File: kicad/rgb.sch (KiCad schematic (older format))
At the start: 3 parts, among them Q1 PMV15ENEA, Q2 PMV15ENEA, U1 ATTINY404-SSNR

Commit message: Starting schematics
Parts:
- removed Q1, Q2: PMV15ENEA, Package_TO_SOT_SMD:SOT-23_Handsoldering, symbol Device:Q_NMOS_GSD
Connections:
- net labels removed: DRAIN_1, DRAIN_2, GND, PWM_1, PWM_2
- wire segments 8 -> 0
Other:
- moved on the sheet: U1
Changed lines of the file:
@@
 Comment4 ""
 $EndDescr
-Wire Wire Line
-	5500 1350 5500 1400
-$Comp
-L power:GND #PWR0101
-U 1 1 5FE3CA70
-P 5500 1400
-F 0 "#PWR0101" H 5500 1150 50  0001 C CNN
-F 1 "GND" H 5505 1227 50  0000 C CNN
-F 2 "" H 5500 1400 50  0001 C CNN
-F 3 "" H 5500 1400 50  0001 C CNN
-	1    5500 1400
-	1    0    0    -1
-$EndComp
-Wire Wire Line
-	5500 950  5500 900
-Wire Wire Line
-	5500 900  6000 900
-Text Label 6000 900  2    50   ~ 0
-DRAIN_1
-Wire Wire Line
-	5500 2350 5500 2400
-$Comp
-L power:GND #PWR0102
-U 1 1 5FE3FFDC
-P 5500 2400
-F 0 "#PWR0102" H 5500 2150 50  0001 C CNN
-F 1 "GND" H 5505 2227 50  0000 C CNN
-F 2 "" H 5500 2400 50  0001 C CNN
-F 3 "" H 5500 2400 50  0001 C CNN
-	1    5500 2400
-	1    0    0    -1
-$EndComp
-Wire Wire Line
-	5500 1950 5500 1900
-Wire Wire Line
-	5500 1900 6000 1900
-Text Label 6000 1900 2    50   ~ 0
-DRAIN_2
-Wire Wire Line
-	4900 2150 5200 2150
-Text Label 4900 2150 0    50   ~ 0
-PWM_2
-$Comp
-L Device:Q_NMOS_GSD Q2
-U 1 1 5FE3FFD3
-P 5400 2150
-F 0 "Q2" H 5605 2196 50  0000 L CNN
-F 1 "PMV15ENEA" H 5605 2105 50  0000 L CNN
-F 2 "Package_TO_SOT_SMD:SOT-23_Handsoldering" H 5600 2250 50  0001 C CNN
-F 3 "https://assets.nexperia.com/documents/data-sheet/PMV15ENEA.pdf" H 5400 2150 50  0001 C CNN
-	1    5400 2150
-	1    0    0    -1
-$EndComp
-Wire Wire Line
-	4900 1150 5200 1150
-Text Label 4900 1150 0    50   ~ 0
-PWM_1
-$Comp
-L Device:Q_NMOS_GSD Q1
-U 1 1 5FE256DE
-P 5400 1150
-F 0 "Q1" H 5605 1196 50  0000 L CNN
-F 1 "PMV15ENEA" H 5605 1105 50  0000 L CNN
-F 2 "Package_TO_SOT_SMD:SOT-23_Handsoldering" H 5600 1250 50  0001 C CNN
-F 3 "https://assets.nexperia.com/documents/data-sheet/PMV15ENEA.pdf" H 5400 1150 50  0001 C CNN
-	1    5400 1150
-	1    0    0    -1
-$EndComp
 $Comp
 L ATTINY404-SSNR:ATTINY404-SSNR U1
 U 1 1 5FE13C65
-P 1490 1450
-F 0 "U1" H 2690 1937 60  0000 C CNN
-F 1 "ATTINY404-SSNR" H 2690 1831 60  0000 C CNN
-F 2 "rgb_footprints:ATTINY404-SSNR" H 2690 1790 60  0001 C CNN
-F 3 "https://ww1.microchip.com/downloads/en/DeviceDoc/ATtiny204-404-DataSheet-DS50002687B.pdf" H 2690 1831 60  0001 C CNN
-	1    1490 1450
+P 840 1600
+F 0 "U1" H 2040 2087 60  0000 C CNN
+F 1 "ATTINY404-SSNR" H 2040 1981 60  0000 C CNN
+F 2 "rgb_footprints:ATTINY404-SSNR" H 2040 1940 60  0001 C CNN
+F 3 "https://ww1.microchip.com/downloads/en/DeviceDoc/ATtiny204-404-DataSheet-DS50002687B.pdf" H 2040 1981 60  0001 C CNN
+	1    840  1600
 	1    0    0    -1
 $EndComp

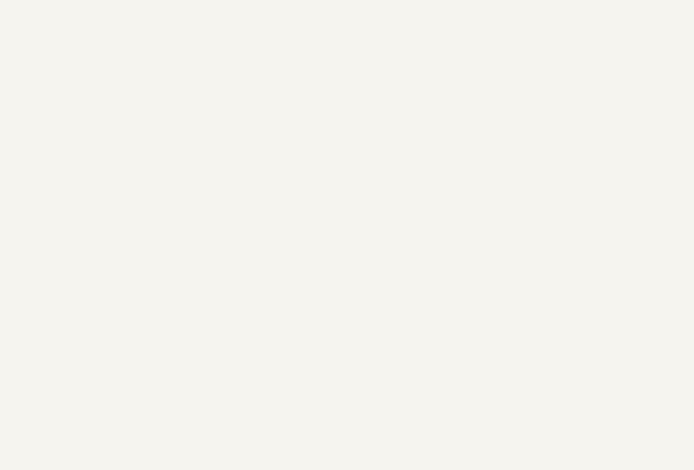
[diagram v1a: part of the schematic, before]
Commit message: changed mosfets
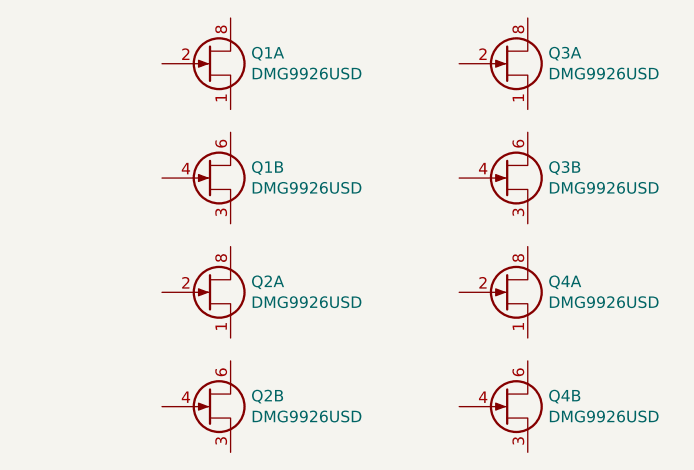
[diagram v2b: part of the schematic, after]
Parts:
- added Q1, Q2, Q3, Q4: DMG9926USD, Package_SO:SO-8_3.9x4.9mm_P1.27mm, symbol mosfet:DMG9926USD
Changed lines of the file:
@@
+	1    0    0    -1
+$EndComp
+$Comp
+L mosfet:DMG9926USD Q1
+U 1 1 5FE90B41
+P 4950 1000
+F 0 "Q1" H 5090 1046 50  0000 L CNN
+F 1 "DMG9926USD" H 5090 955 50  0000 L CNN
+F 2 "Package_SO:SO-8_3.9x4.9mm_P1.27mm" H 4850 500 50  0001 C CNN
+F 3 "https://www.diodes.com/assets/Datasheets/ds31757.pdf" H 4375 1160 50  0001 C CNN
+	1    4950 1000
+	1    0    0    -1
+$EndComp
+$Comp
+L mosfet:DMG9926USD Q1
+U 2 1 5FE91CF3
+P 4950 1500
+F 0 "Q1" H 5090 1546 50  0000 L CNN
+F 1 "DMG9926USD" H 5090 1455 50  0000 L CNN
+F 2 "Package_SO:SO-8_3.9x4.9mm_P1.27mm" H 4850 1000 50  0001 C CNN
+F 3 "https://www.diodes.com/assets/Datasheets/ds31757.pdf" H 4375 1660 50  0001 C CNN
+	2    4950 1500
+	1    0    0    -1
+$EndComp
+$Comp
+L mosfet:DMG9926USD Q2
+U 1 1 5FE99194
+P 4950 2000
+F 0 "Q2" H 5090 2046 50  0000 L CNN
+F 1 "DMG9926USD" H 5090 1955 50  0000 L CNN
+F 2 "Package_SO:SO-8_3.9x4.9mm_P1.27mm" H 4850 1500 50  0001 C CNN
+F 3 "https://www.diodes.com/assets/Datasheets/ds31757.pdf" H 4375 2160 50  0001 C CNN
+	1    4950 2000
+	1    0    0    -1
+$EndComp
+$Comp
+L mosfet:DMG9926USD Q2
+U 2 1 5FE9919A
+P 4950 2500
+F 0 "Q2" H 5090 2546 50  0000 L CNN
+F 1 "DMG9926USD" H 5090 2455 50  0000 L CNN
+F 2 "Package_SO:SO-8_3.9x4.9mm_P1.27mm" H 4850 2000 50  0001 C CNN
+F 3 "https://www.diodes.com/assets/Datasheets/ds31757.pdf" H 4375 2660 50  0001 C CNN
+	2    4950 2500
+	1    0    0    -1
+$EndComp
+$Comp
+L mosfet:DMG9926USD Q3
+U 1 1 5FE9AB06
+P 6250 1000
+F 0 "Q3" H 6390 1046 50  0000 L CNN
+F 1 "DMG9926USD" H 6390 955 50  0000 L CNN
+F 2 "Package_SO:SO-8_3.9x4.9mm_P1.27mm" H 6150 500 50  0001 C CNN
+F 3 "https://www.diodes.com/assets/Datasheets/ds31757.pdf" H 5675 1160 50  0001 C CNN
+	1    6250 1000
+	1    0    0    -1
+$EndComp
+$Comp
+L mosfet:DMG9926USD Q3
+U 2 1 5FE9AB0C
+P 6250 1500
+F 0 "Q3" H 6390 1546 50  0000 L CNN
+F 1 "DMG9926USD" H 6390 1455 50  0000 L CNN
+F 2 "Package_SO:SO-8_3.9x4.9mm_P1.27mm" H 6150 1000 50  0001 C CNN
+F 3 "https://www.diodes.com/assets/Datasheets/ds31757.pdf" H 5675 1660 50  0001 C CNN
+	2    6250 1500
+	1    0    0    -1
+$EndComp
+$Comp
+L mosfet:DMG9926USD Q4
+U 1 1 5FEA036A
+P 6250 2000
+F 0 "Q4" H 6390 2046 50  0000 L CNN
+F 1 "DMG9926USD" H 6390 1955 50  0000 L CNN
+F 2 "Package_SO:SO-8_3.9x4.9mm_P1.27mm" H 6150 1500 50  0001 C CNN
+F 3 "https://www.diodes.com/assets/Datasheets/ds31757.pdf" H 5675 2160 50  0001 C CNN
+	1    6250 2000
+	1    0    0    -1
+$EndComp
+$Comp
+L mosfet:DMG9926USD Q4
+U 2 1 5FEA0370
+P 6250 2500
+F 0 "Q4" H 6390 2546 50  0000 L CNN
+F 1 "DMG9926USD" H 6390 2455 50  0000 L CNN
+F 2 "Package_SO:SO-8_3.9x4.9mm_P1.27mm" H 6150 2000 50  0001 C CNN
+F 3 "https://www.diodes.com/assets/Datasheets/ds31757.pdf" H 5675 2660 50  0001 C CNN
+	2    6250 2500
 	1    0    0    -1
 $EndComp

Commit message: Added power supply
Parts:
- added C1: 10 uF, symbol Device:C_Small
- added C2, C5: 22 uF, symbol Device:C_Small
- added C3: 100 nF, symbol Device:C_Small
- added C4: 100 pF, symbol Device:C_Small
- added L1: 2.2 uF, symbol Device:L_Small
- added R1: 30.9 kΩ, symbol Device:R_Small_US
- added R2: 62 kΩ, symbol Device:R_Small_US
- added U2: AP63205WU-7, SOIC_05WU-7_DIO, symbol AP63205WU:AP63205WU-7
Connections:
- net labels added: GND
- wire segments 0 -> 30
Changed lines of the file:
@@
 	1    0    0    -1
 $EndComp
+$Comp
+L AP63205WU:AP63205WU-7 U2
+U 1 1 5FE8CD56
+P 1650 3450
+F 0 "U2" H 2450 3837 60  0000 C CNN
+F 1 "AP63205WU-7" H 2450 3731 60  0000 C CNN
+F 2 "SOIC_05WU-7_DIO" H 2450 3690 60  0001 C CNN
+F 3 "" H 1650 3450 60  0000 C CNN
+	1    1650 3450
+	1    0    0    -1
+$EndComp
+$Comp
+L Device:R_Small_US R1
+U 1 1 5FE9900A
+P 4600 3400
+F 0 "R1" H 4500 3400 50  0000 R CNN
+F 1 "30.9 kΩ" H 4550 3500 50  0000 R CNN
+F 2 "" H 4600 3400 50  0001 C CNN
+F 3 "~" H 4600 3400 50  0001 C CNN
+	1    4600 3400
+	-1   0    0    1
+$EndComp
+$Comp
+L Device:R_Small_US R2
+U 1 1 5FE9EA80
+P 4600 3750
+F 0 "R2" H 4700 3800 50  0000 L CNN
+F 1 "62 kΩ" H 4668 3705 50  0000 L CNN
+F 2 "" H 4600 3750 50  0001 C CNN
+F 3 "~" H 4600 3750 50  0001 C CNN
+	1    4600 3750
+	1    0    0    -1
+$EndComp
+$Comp
+L Device:C_Small C1
+U 1 1 5FEA05BD
+P 1300 3700
+F 0 "C1" H 1209 3654 50  0000 R CNN
+F 1 "10 uF" H 1209 3745 50  0000 R CNN
+F 2 "" H 1300 3700 50  0001 C CNN
+F 3 "~" H 1300 3700 50  0001 C CNN
+	1    1300 3700
+	1    0    0    1
+$EndComp
+$Comp
+L Device:C_Small C3
+U 1 1 5FEA2171
+P 3400 3500
+F 0 "C3" H 3600 3600 50  0000 L CNN
+F 1 "100 nF" H 3500 3500 50  0000 L CNN
+F 2 "" H 3400 3500 50  0001 C CNN
+F 3 "~" H 3400 3500 50  0001 C CNN
+	1    3400 3500
+	1    0    0    -1
+$EndComp
+$Comp
+L Device:C_Small C2
+U 1 1 5FEA65A3
+P 5050 3600
+F 0 "C2" H 5200 3650 50  0000 C CNN
+F 1 "22 uF" H 5142 3555 50  0000 L CNN
+F 2 "" H 5050 3600 50  0001 C CNN
+F 3 "~" H 5050 3600 50  0001 C CNN
+	1    5050 3600
+	1    0    0    -1
+$EndComp
+$Comp
+L Device:L_Small L1
+U 1 1 5FEA81A8
+P 3950 3600
+F 0 "L1" V 4150 3550 50  0000 C CNN
+F 1 "2.2 uF" V 4050 3550 50  0000 C CNN
+F 2 "" H 3950 3600 50  0001 C CNN
+F 3 "~" H 3950 3600 50  0001 C CNN
+	1    3950 3600
+	0    -1   -1   0
+$EndComp
+Wire Wire Line
+	3250 3450 3250 3400
+Wire Wire Line
+	3250 3400 3400 3400
+Wire Wire Line
+	3250 3550 3250 3600
+Wire Wire Line
+	3250 3600 3400 3600
+Wire Wire Line
+	3400 3600 3850 3600
+Connection ~ 3400 3600
+Wire Wire Line
+	4050 3600 4150 3600
+Wire Wire Line
+	4150 3200 1550 3200
+Wire Wire Line
+	1550 3200 1550 3450
+Wire Wire Line
+	1550 3450 1650 3450
+Wire Wire Line
+	4150 3300 4150 3200
+$Comp
+L Device:C_Small C4
+U 1 1 5FEA44F3
+P 4150 3400
+F 0 "C4" H 4300 3400 50  0000 L CNN
+F 1 "100 pF" H 4250 3300 50  0000 L CNN
+F 2 "" H 4150 3400 50  0001 C CNN
+F 3 "~" H 4150 3400 50  0001 C CNN
+	1    4150 3400
+	1    0    0    -1
+$EndComp
+Wire Wire Line
+	4150 3600 4150 3500
+Wire Wire Line
+	4600 3300 4600 3200
+Wire Wire Line
+	4600 3200 4150 3200
+Connection ~ 4150 3200
+Wire Wire Line
+	4600 3500 4600 3600
+Wire Wire Line
+	4600 3600 4150 3600
+Connection ~ 4150 3600
+Wire Wire Line
+	4600 3600 4600 3650
+Connection ~ 4600 3600
+Wire Wire Line
+	4600 3850 4600 3900
+Wire Wire Line
+	3250 3900 3250 3650
+Wire Wire Line
+	5050 3900 5050 3700
+Wire Wire Line
+	5050 3500 5050 3200
+Wire Wire Line
+	5050 3200 4600 3200
+Connection ~ 4600 3200
+$Comp
+L power:GND #PWR?
+U 1 1 5FEC6718
+P 4600 3900
+F 0 "#PWR?" H 4600 3650 50  0001 C CNN
+F 1 "GND" H 4605 3727 50  0000 C CNN
+F 2 "" H 4600 3900 50  0001 C CNN
+F 3 "" H 4600 3900 50  0001 C CNN
+	1    4600 3900
+	1    0    0    -1
+$EndComp
+$Comp
+L power:GND #PWR?
+U 1 1 5FEC75F4
+P 1300 3900
+F 0 "#PWR?" H 1300 3650 50  0001 C CNN
+F 1 "GND" H 1305 3727 50  0000 C CNN
+F 2 "" H 1300 3900 50  0001 C CNN
+F 3 "" H 1300 3900 50  0001 C CNN
+	1    1300 3900
+	1    0    0    -1
+$EndComp
+Wire Wire Line
+	1300 3600 1300 3550
+Wire Wire Line
+	1300 3550 1600 3550
+Wire Wire Line
+	1600 3550 1600 3650
+Wire Wire Line
+	1600 3650 1650 3650
+Connection ~ 1600 3550
+Wire Wire Line
+	1600 3550 1650 3550
+$Comp
+L power:GND #PWR?
+U 1 1 5FEC9F13
+P 3250 3900
+F 0 "#PWR?" H 3250 3650 50  0001 C CNN
+F 1 "GND" H 3255 3727 50  0000 C CNN
+F 2 "" H 3250 3900 50  0001 C CNN
+F 3 "" H 3250 3900 50  0001 C CNN
+	1    3250 3900
+	1    0    0    -1
+$EndComp
+Wire Wire Line
+	1300 3800 1300 3900
+$Comp
+L power:GND #PWR?
+U 1 1 5FECCA07
+P 5050 3900
+F 0 "#PWR?" H 5050 3650 50  0001 C CNN
+F 1 "GND" H 5055 3727 50  0000 C CNN
+F 2 "" H 5050 3900 50  0001 C CNN
+F 3 "" H 5050 3900 50  0001 C CNN
+	1    5050 3900
+	1    0    0    -1
+$EndComp
+$Comp
+L Device:C_Small C5
+U 1 1 5FEDA42E
+P 5450 3600
+F 0 "C5" H 5550 3650 50  0000 L CNN
+F 1 "22 uF" H 5542 3555 50  0000 L CNN
+F 2 "" H 5450 3600 50  0001 C CNN
+F 3 "~" H 5450 3600 50  0001 C CNN
+	1    5450 3600
+	1    0    0    -1
+$EndComp
+Wire Wire Line
+	5450 3900 5450 3700
+Wire Wire Line
+	5450 3500 5450 3200
+Wire Wire Line
+	5450 3200 5050 3200
+$Comp
+L power:GND #PWR?
+U 1 1 5FEDA437
+P 5450 3900
+F 0 "#PWR?" H 5450 3650 50  0001 C CNN
+F 1 "GND" H 5455 3727 50  0000 C CNN
+F 2 "" H 5450 3900 50  0001 C CNN
+F 3 "" H 5450 3900 50  0001 C CNN
+	1    5450 3900
+	1    0    0    -1
+$EndComp
+Connection ~ 5050 3200
 $EndSCHEMATC

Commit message: Cleaned up DC-DC
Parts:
- removed C4: 100 pF, symbol Device:C_Small
- removed L1: 2.2 uF, symbol Device:L_Small
- removed R2: 62 kΩ, symbol Device:R_Small_US
- added D1: LED, symbol Device:LED
- added L1: 4.7 uH, symbol Device:L
- R1: value 30.9 kΩ -> 1 kΩ
- renumbered C5 to C3
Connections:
- net labels added: +12V, +5V
- wire segments 30 -> 31
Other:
- note added: "DC-DC converter for MCU"
- moved on the sheet: C1, C2, C3, Q1A, Q1B, Q2A, Q2B, Q3A, Q3B, Q4A, Q4B, U1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

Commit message: driver circuits
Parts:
- removed unit 2 of Q2
- removed unit 2 of Q3
- added unit 2 of Q3 (x2)
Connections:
- net GND: now also Q1.1 (S1), Q1.3 (S2), Q2.1 (S1), Q3.1 (S1), Q4.1 (S1), Q4.3 (S2), Q3.3 (S2), Q3.3 (S2)
- net PWM_1: now reaches Q1.2 (G1)
- net DRAIN_1: now reaches Q1.8 (D1)
- net PWM_2: now reaches Q1.4 (G2)
- net DRAIN_2: now reaches Q1.6 (D2)
- net PWM_3: now reaches Q2.2 (G1)
- net DRAIN_3: now reaches Q2.8 (D1)
- net PWM_5: now reaches Q3.2 (G1)
- net DRAIN_5: now reaches Q3.8 (D1)
- net PWM_7: now reaches Q4.2 (G1)
- net DRAIN_7: now reaches Q4.8 (D1)
- net PWM_8: now reaches Q4.4 (G2)
- net DRAIN_8: now reaches Q4.6 (D2)
- new net DRAIN_4: Q3.6 (D2)
- new net DRAIN_6: Q3.6 (D2)
- new net PWM_4: Q3.4 (G2)
- new net PWM_6: Q3.4 (G2)
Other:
- note added: "Driver Mosfets"
- moved on the sheet: Q1A, U1

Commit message: ATTINY216
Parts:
- removed U1: ATTINY404-SSNR, rgb_footprints:ATTINY404-SSNR, symbol ATTINY404-SSNR:ATTINY404-SSNR
- added C5: 100 nF, symbol Device:C_Small
- added R1: 50 kΩ, symbol Device:R_Small_US
- added SW1, SW2, SW3, SW4: Rotary_Encoder, symbol Device:Rotary_Encoder
- added SW5: SW_Push, symbol Switch:SW_Push
- added SW_PWR: 1825232-1, symbol Switch:SW_SPST
- added U1: ATtiny416-SNR, Package_SO:SOIC-20W_7.5x12.8mm_P1.27mm, symbol MCU_Microchip_ATtiny:ATtiny416-S
- renumbered C3 to C2, C2 to C3, C3 to C4, Q3 to Q2
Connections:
- net +12V: now also SW_PWR.1 (A); no longer U2.2 (EN)
- net +5V: now also C5.1, U1.1 (VCC)
- net GND: now also C5.2, R1.2, SW1.C, SW2.C, SW3.C, SW4.C, SW5.1, U1.20 (GND)
- net PWM_1: now also U1.11 (PB0)
- net PWM_2: now also U1.10 (PB1)
- net PWM_3: now also U1.9 (PB2)
- net PWM_4: now also U1.19 (PA3)
- net PWM_7: now also U1.12 (PC0)
- net PWM_8: now also U1.13 (PC1)
- new net: R1.1, SW_PWR.2 (B), U2.2 (EN)
- new net SW1_A: SW1.A, U1.2 (PA4)
- new net SW2_A: SW2.A, U1.3 (PA5)
- new net SW3_A: SW3.A, U1.4 (PA6)
- new net SW4_A: SW4.A, U1.5 (PA7)
- new net SW5: SW5.2, U1.18 (PA2)
- new net SW_B: SW1.B, SW2.B, SW3.B, SW4.B, U1.17 (PA1)
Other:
- note added: "5V DC-DC converter"
- note added: "Note:\nPlace C5 as close to\nVDD as possible"
- note added: "Rotary Encoders (Common B)"
- note removed: "DC-DC converter for MCU"
- moved on the sheet: C1, C2, C3, C4, D1, L1, Q1A, Q1B, Q2A, Q2B, Q3A, Q3B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

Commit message: Schematics work
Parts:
- removed unit 1 of Q3
- removed unit 1 of Q4
- removed R1: 50 kΩ, symbol Device:R_Small_US
- removed SW_PWR: 1825232-1, symbol Switch:SW_SPST
- added F1: 0685H9200-01, Fuse:Fuse_1206_3216Metric_Pad1.42x1.75mm_HandSolder, symbol Device:Fuse
- added J1: 1935776, symbol Connector_Generic:Conn_01x02
- added J2, J3: Conn_01x05, symbol Connector_Generic:Conn_01x05
- added J4: Conn_01x04, symbol Connector_Generic:Conn_01x03
- added J5: Conn_01x02, symbol Connector_Generic:Conn_01x04
- added unit 2 of Q1
- added unit 2 of Q2
- added R1: 1 kΩ, symbol Device:R_Small_US
- added R1: 60k, symbol Device:R_Small_US
- added R2: 10k, symbol Device:R_Small_US
- added SW1: 1825232-1, rgb_footprints:Switch_Slide_1825232-1, symbol Switch:SW_SPDT
- Q1, Q3, Q4: footprint Package_SO:SO-8_3.9x4.9mm_P1.27mm -> rgb_footprints:DMG9926USD_Handsolder
- Q2: renamed from Q1; footprint Package_SO:SO-8_3.9x4.9mm_P1.27mm -> rgb_footprints:DMG9926USD_Handsolder
- Q3, Q4: renamed from Q2; footprint Package_SO:SO-8_3.9x4.9mm_P1.27mm -> rgb_footprints:DMG9926USD_Handsolder
- U1: footprint Package_SO:SOIC-20W_7.5x12.8mm_P1.27mm -> rgb_footprints:ATTINY416-SNR
- U2: footprint SOIC_05WU-7_DIO -> rgb_footprints:AP63205WU-7
- renumbered R1 to R2, SW1 to SW2, SW2 to SW3, SW3 to SW4, SW4 to SW5, SW5 to SW6
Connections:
- net +12V: now also F1.1, J2.1 (Pin_1), J3.1 (Pin_1), R1.1, SW1.1 (A)
- net +5V: now also U2.1 (FB), J4.3 (Pin_3), J5.4 (Pin_4)
- net DRAIN_1: now also J2.2 (Pin_2)
- net DRAIN_2: now also J2.3 (Pin_3), Q1.6 (D2); no longer Q2.6 (D2)
- net DRAIN_3: now also Q2.8 (D1), J2.4 (Pin_4); no longer Q3.8 (D1)
- net DRAIN_4: now also J2.5 (Pin_5), Q2.6 (D2); no longer Q4.6 (D2)
- net DRAIN_5: now also Q3.8 (D1), J3.2 (Pin_2)
- net DRAIN_6: now also J3.3 (Pin_3)
- net DRAIN_7: now also Q4.8 (D1), J3.4 (Pin_4)
- net DRAIN_8: now also J3.5 (Pin_5)
- net GND: now also Q2.1 (S1), Q4.1 (S1), J1.1 (Pin_1), J4.1 (Pin_1), J5.1 (Pin_1), Q1.3 (S2), Q2.3 (S2), R1.2, R2.2; no longer Q2.3 (S2), Q4.3 (S2)
- net PWM_2: now also Q1.4 (G2); no longer Q2.4 (G2)
- net PWM_3: now also Q2.2 (G1); no longer Q3.2 (G1)
- net PWM_4: now also Q2.4 (G2); no longer Q4.4 (G2)
- net PWM_5: now also Q3.2 (G1), U1.2 (PA4)
- net PWM_6: now also U1.3 (PA5)
- net PWM_7: now also Q4.2 (G1)
- net SW2_A: now also SW2.A, U1.14 (PC2); no longer SW3.A, U1.3 (PA5)
- net SW3_A: now also SW3.A, U1.15 (PC3); no longer SW4.A, U1.4 (PA6)
- net SW4_A: now also SW4.A, U1.4 (PA6); no longer SW5.A, U1.5 (PA7)
- net SW_B: now also U1.8 (PB3); no longer U1.17 (PA1)
- net at C2.2, L1.1, U2.5 (SW): no longer U2.1 (FB)
- net at U2.2 (EN): now also SW1.2 (B)
- net RESET: now reaches U1.16 (~RESET~/PA0)
- net RESET: now also J4.2 (Pin_2)
- net VIN_ADC: now reaches U1.6 (PB5)
- net VIN_ADC: now also R1.2, R2.1
- net SW6: now reaches U1.7 (PB4)
- net SW6: now also SW6.2
- removed net SW1_A: SW2.A, U1.2 (PA4)
- net SW5 renamed TWI_SCL
- net TWI_SCL: now also J5.2 (Pin_2); no longer SW6.2
- new net: R1.1, SW1.3 (C)
- new net: F1.2, J1.2 (Pin_2)
- new net SW5_A: SW5.A, U1.5 (PA7)
- new net TWI_SDA: J5.3 (Pin_3), U1.17 (PA1)
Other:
- note added: "Channel 1"
- note added: "Channel 2\n"
- note added: "Channel select\n"
- note added: "DC-DC Converter"
- note added: "DMG9926USD (2 n-channel / chip)"
- note added: "LED Driver Mosfets"
- note added: "Layout:\nPlace C5 as close to VDD as possible (refer to AVR040 4.6)"
- note added: "MCU"
- note added: "Physical Controls"
- note added: "Power"
- note added: "Programming"
- note added: "Protection / Connectors\n"
- note added: "Quadrature rotary encoders"
- note added: "TWI Slave"
- note removed: "5V DC-DC converter"
- note removed: "Driver Mosfets"
- note removed: "Note:\nPlace C5 as close to\nVDD as possible"
- note removed: "Rotary Encoders (Common B)"
- moved on the sheet: C1, C2, C3, C4, C5, D1, L1, Q1A, Q3A, R2, SW2, SW3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

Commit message: Connectors / protection
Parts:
- removed R1: 1 kΩ, symbol Device:R_Small_US
- removed R1: 60k, symbol Device:R_Small_US
- removed SW1: 1825232-1, rgb_footprints:Switch_Slide_1825232-1, symbol Switch:SW_SPDT
- added R1: 15 kΩ, symbol Device:R_Small_US
- added SW1: SW_Push, symbol Switch:SW_Push
- R2: value 10k -> 10 kΩ
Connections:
- net +12V: now also SW1.1
- net VIN_ADC: no longer R2.1, U1.6 (PB5)
- net PWR_EN: now reaches U2.2 (EN)
- net PWR_EN: now also R2.1, U1.6 (PB5), R1.2
- new net: R1.1, SW1.2
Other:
- moved on the sheet: C1, C2, C3, C4, C5, D1, L1, R2, SW6, U1, U2
